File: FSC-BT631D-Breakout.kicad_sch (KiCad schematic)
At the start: 0 parts

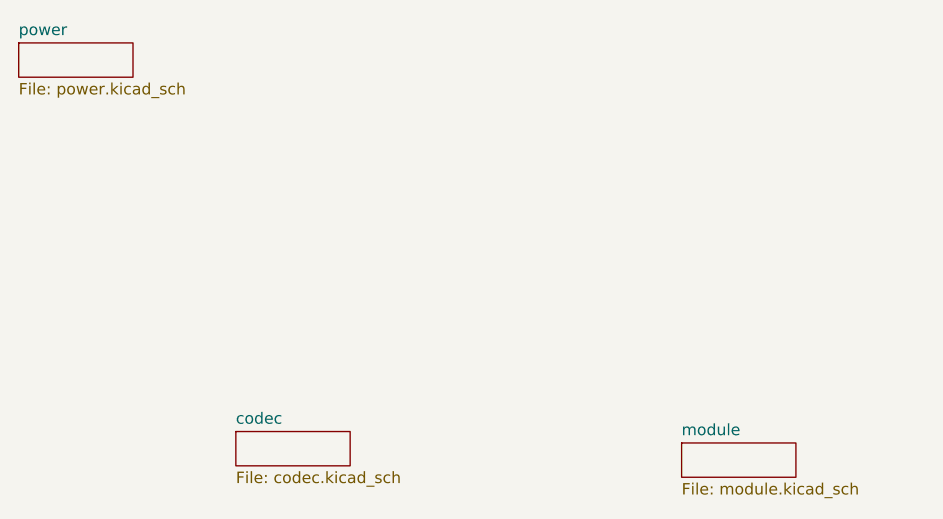
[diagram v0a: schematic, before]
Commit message: fixed ground pour
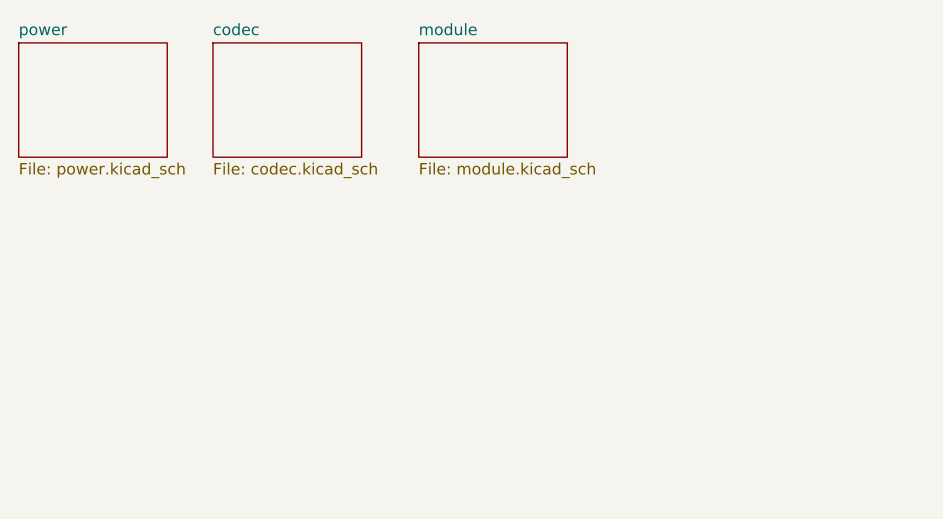
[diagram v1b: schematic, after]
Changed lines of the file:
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@@
 	(paper "A4")
 	(sheet
-		(at 132.08 107.95)
-		(size 12.7 3.81)
+		(at 102.87 63.5)
+		(size 16.51 12.7)
 		(exclude_from_sim no)
 		(in_bom yes)
@@
 		)
 		(property "Sheetname" "module"
-			(at 132.08 107.2384 0)
+			(at 102.87 62.7884 0)
 			(effects
 				(font
@@
 		)
 		(property "Sheetfile" "module.kicad_sch"
-			(at 132.08 112.3446 0)
+			(at 102.87 76.7846 0)
 			(effects
 				(font
@@
 	(sheet
 		(at 58.42 63.5)
-		(size 12.7 3.81)
+		(size 16.51 12.7)
 		(exclude_from_sim no)
 		(in_bom yes)
@@
 		)
 		(property "Sheetfile" "power.kicad_sch"
-			(at 58.42 67.8946 0)
+			(at 58.42 76.7846 0)
 			(effects
 				(font
@@
 	)
 	(sheet
-		(at 82.55 106.68)
-		(size 12.7 3.81)
+		(at 80.01 63.5)
+		(size 16.51 12.7)
 		(exclude_from_sim no)
 		(in_bom yes)
@@
 		)
 		(property "Sheetname" "codec"
-			(at 82.55 105.9684 0)
+			(at 80.01 62.7884 0)
 			(effects
 				(font
@@
 		)
 		(property "Sheetfile" "codec.kicad_sch"
-			(at 82.55 111.0746 0)
+			(at 80.01 76.7846 0)
 			(effects
 				(font

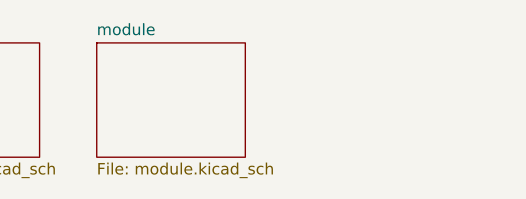
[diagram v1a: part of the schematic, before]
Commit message: added dsp schematic
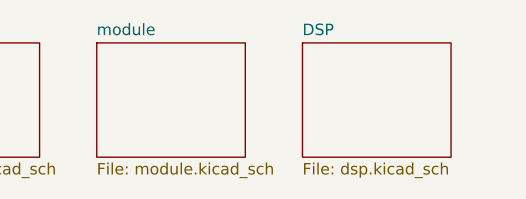
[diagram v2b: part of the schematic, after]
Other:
- added sheet DSP (dsp.kicad_sch)
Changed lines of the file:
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@@
 	(paper "A4")
+	(sheet
+		(at 125.73 63.5)
+		(size 16.51 12.7)
+		(exclude_from_sim no)
+		(in_bom yes)
+		(on_board yes)
+		(dnp no)
+		(fields_autoplaced yes)
+		(stroke
+			(width 0.1524)
+			(type solid)
+		)
+		(fill
+			(color 0 0 0 0.0000)
+		)
+		(property "Sheetname" "DSP"
+			(at 125.73 62.7884 0)
+			(effects
+				(font
+					(size 1.27 1.27)
+				)
+				(justify left bottom)
+			)
+		)
+		(property "Sheetfile" "dsp.kicad_sch"
+			(at 125.73 76.7846 0)
+			(effects
+				(font
+					(size 1.27 1.27)
+				)
+				(justify left top)
+			)
+		)
+		(instances
+			(project "FSC-BT631D-Breakout"
+				(path "/484c4955-80b8-457c-864e-1c65a3218727"
+					(page "6")
+				)
+			)
+		)
+	)
 	(sheet
 		(at 102.87 63.5)
